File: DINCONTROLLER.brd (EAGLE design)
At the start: 102 x 42 mm, 44 parts, among them IC1 ESPWROOM32, SW1 TAC-SWITCH-LEDSP0620, SW2 TAC-SWITCH-LEDSP0620, SW3 TAC-SWITCH-LEDSP0620, SW4 TAC-SWITCH-LEDSP0620, SW5 TAC-SWITCH-LEDSP0620, SW6 TAC-SWITCH-LEDSP0620, SW7 TAC-SWITCH-LEDSP0620, SW8 TAC-SWITCH-LEDSP0620

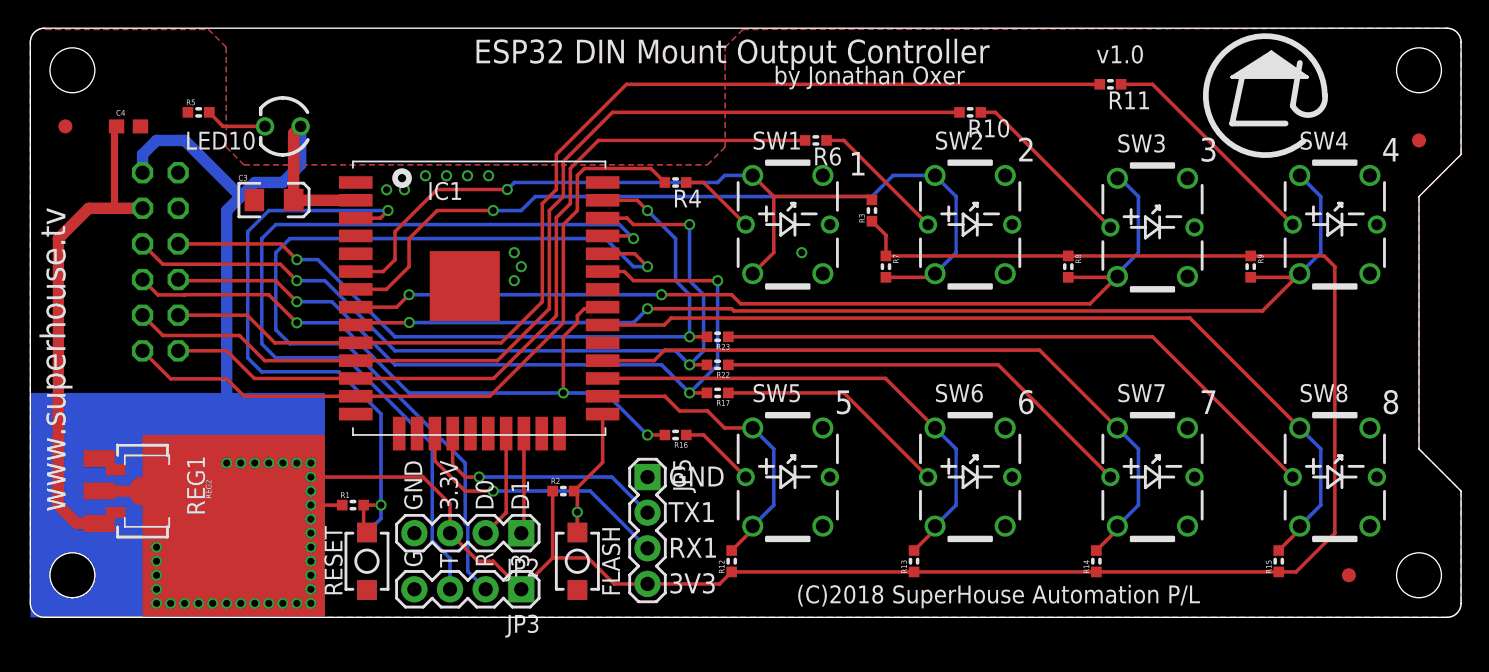
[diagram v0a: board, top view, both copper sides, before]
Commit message: Improved designators
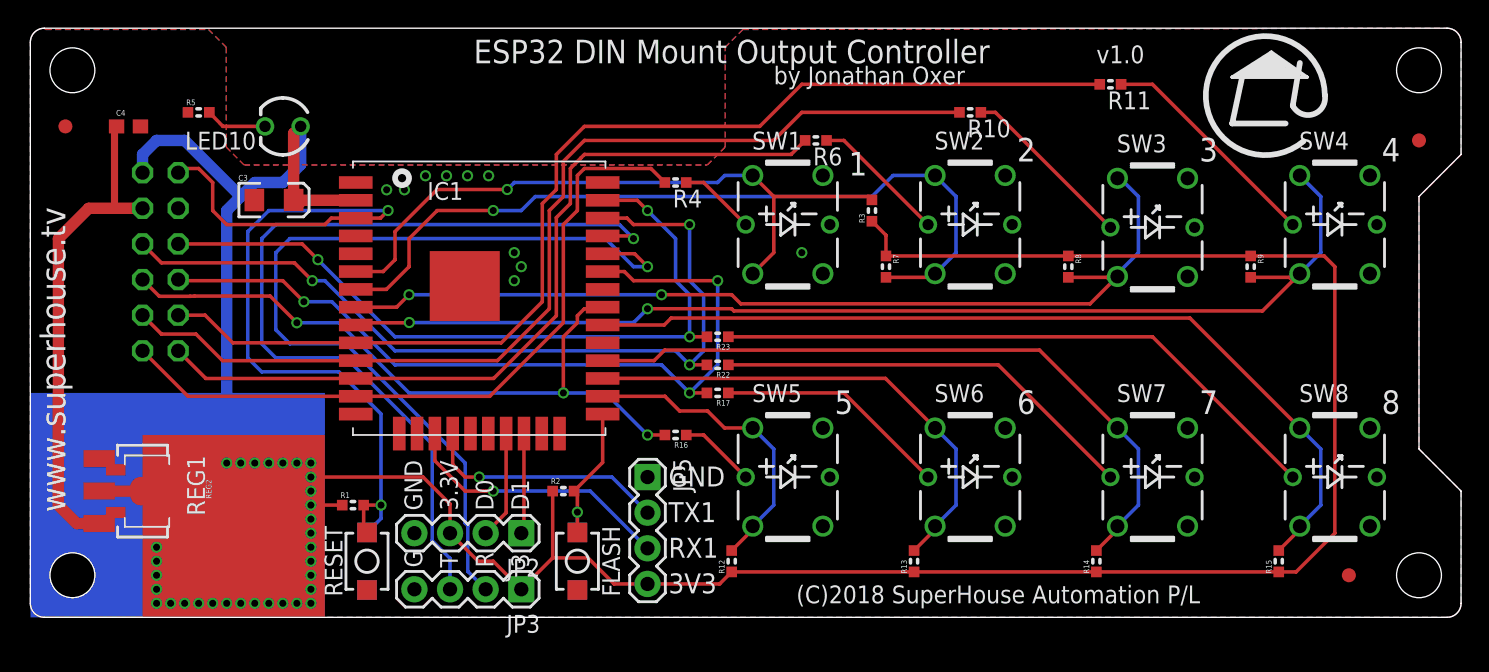
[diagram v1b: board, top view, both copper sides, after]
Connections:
- removed net RESET: JP1.12
- net EN: now also JP1.12
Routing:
- net EN: track 45.5 -> 61.3 mm
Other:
- board text removed: "Arduino IDE Board Profile: ESP32"

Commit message: Major update: remapped IO pins for v1.1 release
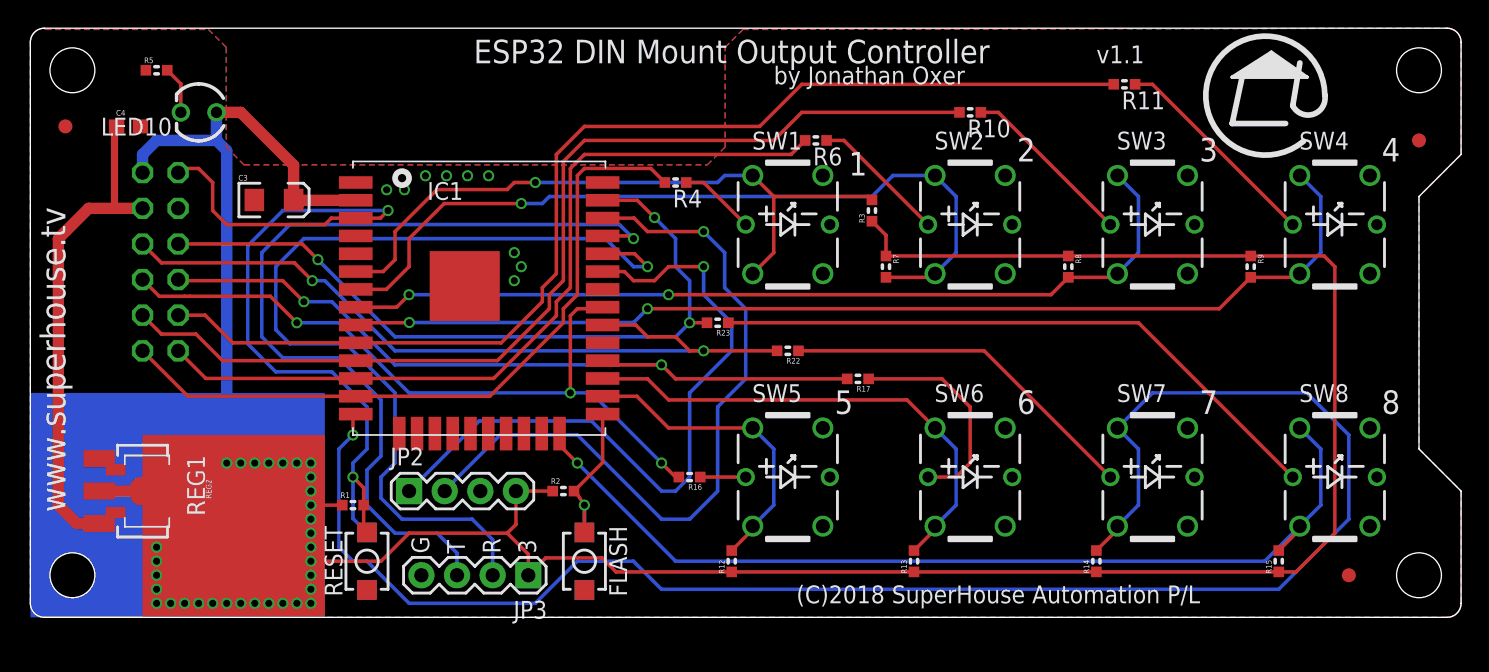
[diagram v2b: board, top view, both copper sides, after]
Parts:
- removed JP5: (no value), freetronics-jon:1X04
- moved R17 10.0 mm to (59.0, 17.0)
- moved JP2 8.54 mm to (27.0, 9.00), turned to 0 degrees
- moved LED10 6.08 mm to (12.0, 36.0)
- moved R22 5.10 mm to (54.0, 19.0)
- moved R5 4.24 mm to (9.00, 39.0)
- moved R16 3.16 mm to (47.0, 10.0)
- moved JP3 1.12 mm to (35.5, 3.00)
- moved R11 1.00 mm to (78.0, 38.0)
- moved R23 1.00 mm to (49.0, 21.0)
- moved S2 0.50 mm to (39.5, 4.00)
- moved S4 0.50 mm to (39.5, 4.00)
- moved SW3 0.20 mm to (80.0, 28.0)
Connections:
- removed net I2C_D0: IC1.21, JP2.2
- removed net I2C_D1: IC1.22, JP2.1
- removed net N$20: IC1.4
- removed net N$21: IC1.5
- removed net RXD1: IC1.17, JP5.3
- removed net TXD1: IC1.18, JP5.2
- new net GPIO21_SDA: IC1.33, JP2.1
- new net GPIO22_SCL: IC1.36, JP2.2
- net 3.3V: now also JP2.4; no longer JP2.3, JP5.4
- net BUTTON7: now also IC1.14; no longer IC1.28
- net BUTTON8: now also IC1.24; no longer IC1.30
- net DATA6: now also IC1.28; no longer IC1.33
- net DATA7: now also IC1.30; no longer IC1.36
- net GND: now also JP2.3; no longer JP2.4, JP5.1
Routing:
- net BUTTON7: track 49.9 -> 123.2 mm, vias 0 -> 1
- net GPIO22_SCL: track 0.00 -> 52.6 mm, vias 0 -> 1
- net GPIO21_SDA: track 0.00 -> 49.5 mm, vias 0 -> 1
- net RXD1: track 19.7 -> 0.00 mm, vias 1 -> 0
- net TXD1: track 17.5 -> 0.00 mm, vias 1 -> 0
- net I2C_D0: track 7.70 -> 0.00 mm
- net I2C_D1: track 7.18 -> 0.00 mm
- net 3.3V: track 251.7 -> 246.7 mm
- net BUTTON8: track 63.8 -> 68.7 mm, vias 0 -> 1
- net DATA7: track 61.0 -> 56.4 mm, vias 3 -> 2
- net N$23: track 30.6 -> 26.0 mm
- net BUTTON3: track 67.3 -> 63.6 mm
- net DATA6: track 58.3 -> 55.0 mm, vias 3 -> 2
- net BUTTON4: track 80.3 -> 77.1 mm
- net RXD0: track 63.9 -> 66.2 mm
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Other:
- board text added: "A"
- board text added: "Button 1: IO34 Button 2: IO35 Button 3: IO32 Button 4: IO33 Button 5: IO4 Button 6: IO16 Button 7: IO12 Button 8: IO2"
- board text added: "I2C"
- board text added: "L"
- board text added: "Output1: IO14 Output2: IO27 Output3: IO26 Output4: IO25 Output5: IO19 Output6: IO17 Output7: IO18 Output8: IO23"
- board text added: "PROG"
- board text added: "v1.1"
- board text removed: "3.3V"
- board text removed: "3V3"
- board text removed: "Button 1: IO34 Button 2: IO35 Button 3: IO32 Button 4: IO33 Button 5: IO4 Button 6: IO16 Button 7: IO17 Button 8: IO18"
- board text removed: "D0"
- board text removed: "Output1: IO14 Output2: IO27 Output3: IO26 Output4: IO25 Output5: IO19 Output6: IO21 Output7: IO22 Output8: IO23"
- board text removed: "RX1"
- board text removed: "TX1"
- board text removed: "v1.0"
